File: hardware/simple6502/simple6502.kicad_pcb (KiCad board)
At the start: 2 copper layers, 100 x 100 mm, 37 parts, among them J1 ~{VP}, J2 CLK SEL, J3 RESET, J5 POWER 5V, J6 AUX 5VDC, SW1 RESET, SW2 POWER, T1 DS1813-10+, U1 W65C02SxP, U2 CY62256-70PC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

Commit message: First PCB Layout
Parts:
- moved U4 139.9 mm to (62.4, 115.5)
- moved U5 139.6 mm to (62.3, 102.6)
- moved C7 86.4 mm to (116.5, 54.0), turned to 180 degrees
- moved C6 86.1 mm to (124.0, 83.0), turned to -90 degrees
- moved TP3 74.5 mm to (114.0, 145.0)
- moved C3 64.5 mm to (82.5, 120.5), turned to -90 degrees
- moved C2 54.4 mm to (86.8, 94.0)
- moved C1 53.5 mm to (55.5, 74.0)
- moved TP1 49.0 mm to (134.0, 119.0)
- moved J2 47.7 mm to (141.0, 119.0), turned to 90 degrees
- moved TP2 47.6 mm to (137.0, 54.5)
- moved R3 45.0 mm to (117.0, 70.2), turned to -90 degrees
- moved R2 40.5 mm to (120.5, 70.2), turned to -90 degrees
- moved C5 31.5 mm to (55.8, 108.0)
- moved R5 30.3 mm to (147.5, 67.6), turned to 90 degrees
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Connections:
- net Net-(U1-BE) renamed /BE
- net Net-(U1-~{SO}) renamed /~{SO}
- R3 pad 1: VCC -> /RDY
- R3 pad 2: Net-(U1-RDY) -> VCC
- U1 pad 2: Net-(U1-RDY) -> /RDY

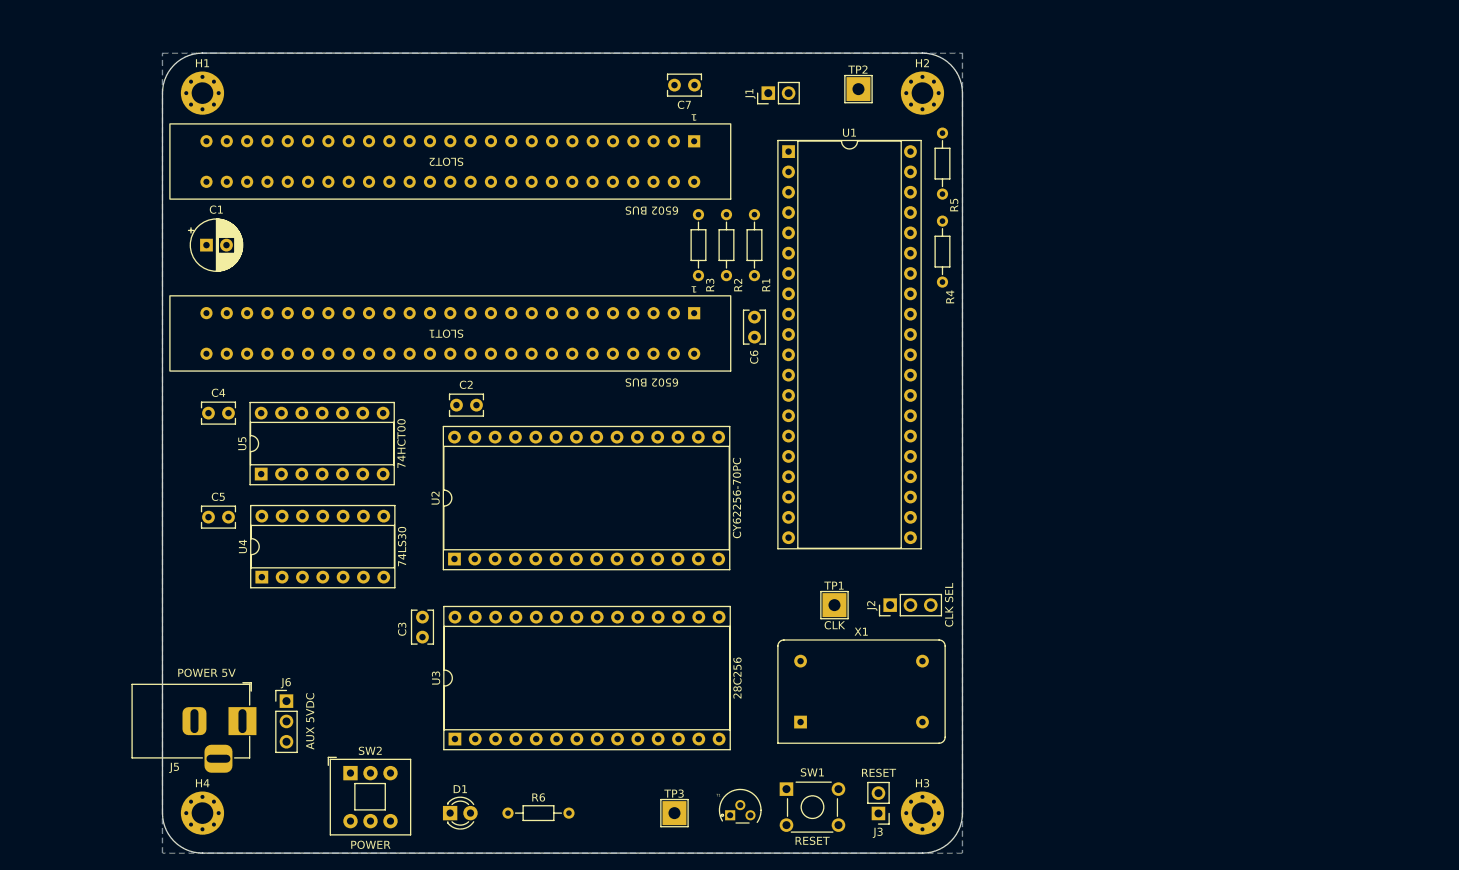
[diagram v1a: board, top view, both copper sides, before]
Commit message: Fixed Apple Connector 3D model, routing started
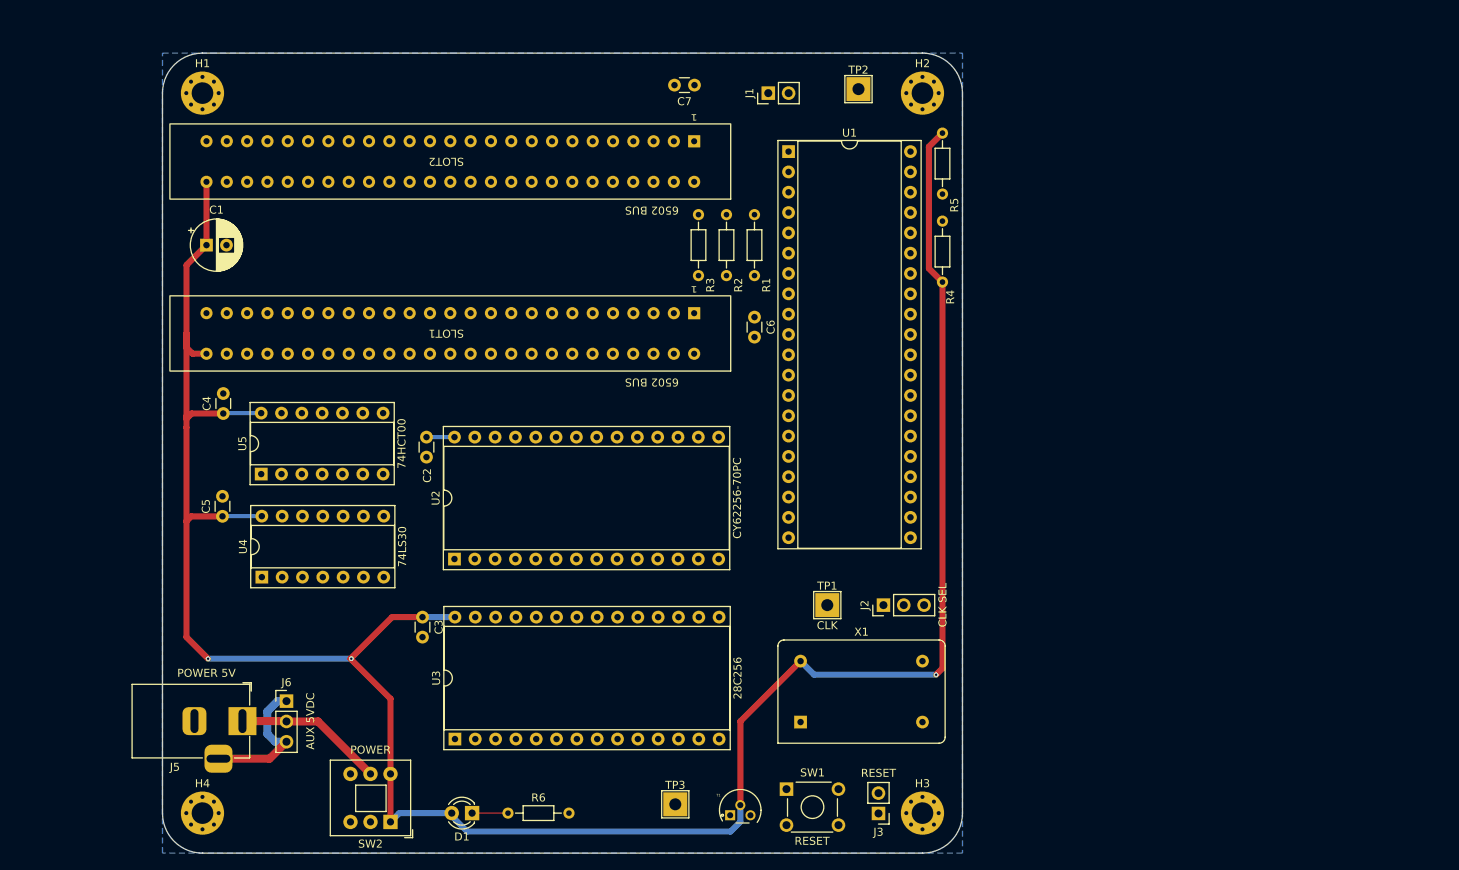
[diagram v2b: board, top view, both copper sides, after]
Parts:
- C2, C3, C4, C5, C6, C7: footprint Capacitor_THT:C_Rect_L4.0mm_W2.5mm_P2.50mm -> Capacitor_THT:C_Disc_D3.0mm_W1.6mm_P2.50mm
- moved SW2 7.89 mm to (78.5, 146.1), turned to 180 degrees
- moved C2 5.48 mm to (83.0, 98.0), turned to -90 degrees
- moved D1 2.74 mm to (88.7, 145.0), turned to 180 degrees
- moved C4 1.85 mm to (57.6, 95.0), turned to 90 degrees
- moved C5 1.75 mm to (57.5, 107.9), turned to 90 degrees
- moved TP3 1.10 mm to (114.1, 143.9)
- moved TP1 0.90 mm to (133.1, 119.0)
- moved J2 0.84 mm to (140.1, 119.0)
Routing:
- net VCC: track 0.00 -> 300.9 mm, vias 0 -> 3
- net /Power and support/5VDC IN: track 0.00 -> 18.7 mm
- net /Power and support/AUX GND: track 0.00 -> 17.9 mm
- net Net-(D1-K): track 0.00 -> 4.49 mm

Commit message: Routing PCB
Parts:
- moved C6 2.30 mm to (124.0, 80.7)
- moved R4 1.50 mm to (147.5, 72.5)
- moved R5 0.22 mm to (147.5, 67.4)
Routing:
- net A10: track 0.00 -> 80.1 mm, vias 0 -> 2
- net A11: track 0.00 -> 77.9 mm, vias 0 -> 2
- net A13: track 0.00 -> 75.2 mm, vias 0 -> 1
- net CLK: track 0.00 -> 73.0 mm
- net A8: track 0.00 -> 72.4 mm, vias 0 -> 2
- net A14: track 0.00 -> 70.7 mm
- net A9: track 0.00 -> 70.1 mm, vias 0 -> 2
- net A12: track 0.00 -> 66.8 mm, vias 0 -> 1
- net VCC: track 300.9 -> 347.4 mm
- net D7: track 0.00 -> 46.2 mm
- net A1: track 0.00 -> 45.8 mm
- net D5: track 0.00 -> 45.7 mm
- net D4: track 0.00 -> 45.7 mm
- net ~{RD}: track 0.00 -> 45.7 mm
- net D3: track 0.00 -> 45.7 mm
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
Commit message: More PCB Routing
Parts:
- moved J3 88.3 mm to (139.8, 56.7)
- moved R6 29.4 mm to (66.4, 132.8), turned to 90 degrees
- moved TP3 25.1 mm to (139.2, 142.7)
- moved D1 21.1 mm to (71.5, 132.8), turned to 0 degrees
- moved J6 10.2 mm to (62.0, 140.6)
- moved C3 9.16 mm to (83.0, 111.3)
- moved U3 9.14 mm to (86.6, 126.6)
- moved SW1 8.06 mm to (134.4, 146.9), turned to 180 degrees
- moved U4 7.97 mm to (55.8, 111.1)
- moved U5 7.25 mm to (55.8, 99.5)
- moved C5 6.40 mm to (52.9, 103.5), turned to -90 degrees
- moved C2 6.15 mm to (82.9, 91.8)
- moved U2 6.14 mm to (86.5, 107.1)
- moved C4 5.66 mm to (52.9, 91.9), turned to -90 degrees
- moved SW2 3.50 mm to (75.2, 145.1)
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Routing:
- net ~{RESET}: track 29.7 -> 130.1 mm
- net D6: track 22.3 -> 99.9 mm, vias 0 -> 2
- net A14: track 70.7 -> 122.3 mm, vias 0 -> 2
- net D2: track 45.6 -> 94.1 mm, vias 0 -> 2
- net D7: track 46.2 -> 94.6 mm, vias 0 -> 2
- net D5: track 45.7 -> 92.8 mm, vias 0 -> 2
- net D4: track 45.7 -> 92.7 mm, vias 0 -> 2
- net D1: track 45.6 -> 90.5 mm, vias 0 -> 2
- net D3: track 45.7 -> 90.4 mm, vias 0 -> 1
- net A7: track 45.7 -> 87.2 mm, vias 0 -> 1
- net D0: track 45.6 -> 86.0 mm, vias 0 -> 2
- net A6: track 45.7 -> 82.6 mm, vias 0 -> 1
- net A5: track 45.7 -> 78.3 mm, vias 0 -> 1
- net A11: track 77.9 -> 49.0 mm, vias 2 -> 0
- net A4: track 45.7 -> 73.8 mm, vias 0 -> 1
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
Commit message: Much More PCB Routing - Clean DRC
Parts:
- T1: value DS1813-10+ -> DS1813
- moved C1 0.96 mm to (55.4, 73.0), turned to -90 degrees
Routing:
- net GND: track 22.4 -> 0.00 mm
- net VCC: track 366.9 -> 368.3 mm
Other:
- board text added: "5V"
- board text added: "GND"
- board text added: "SW-G"
- board text added: "~{RESET}"

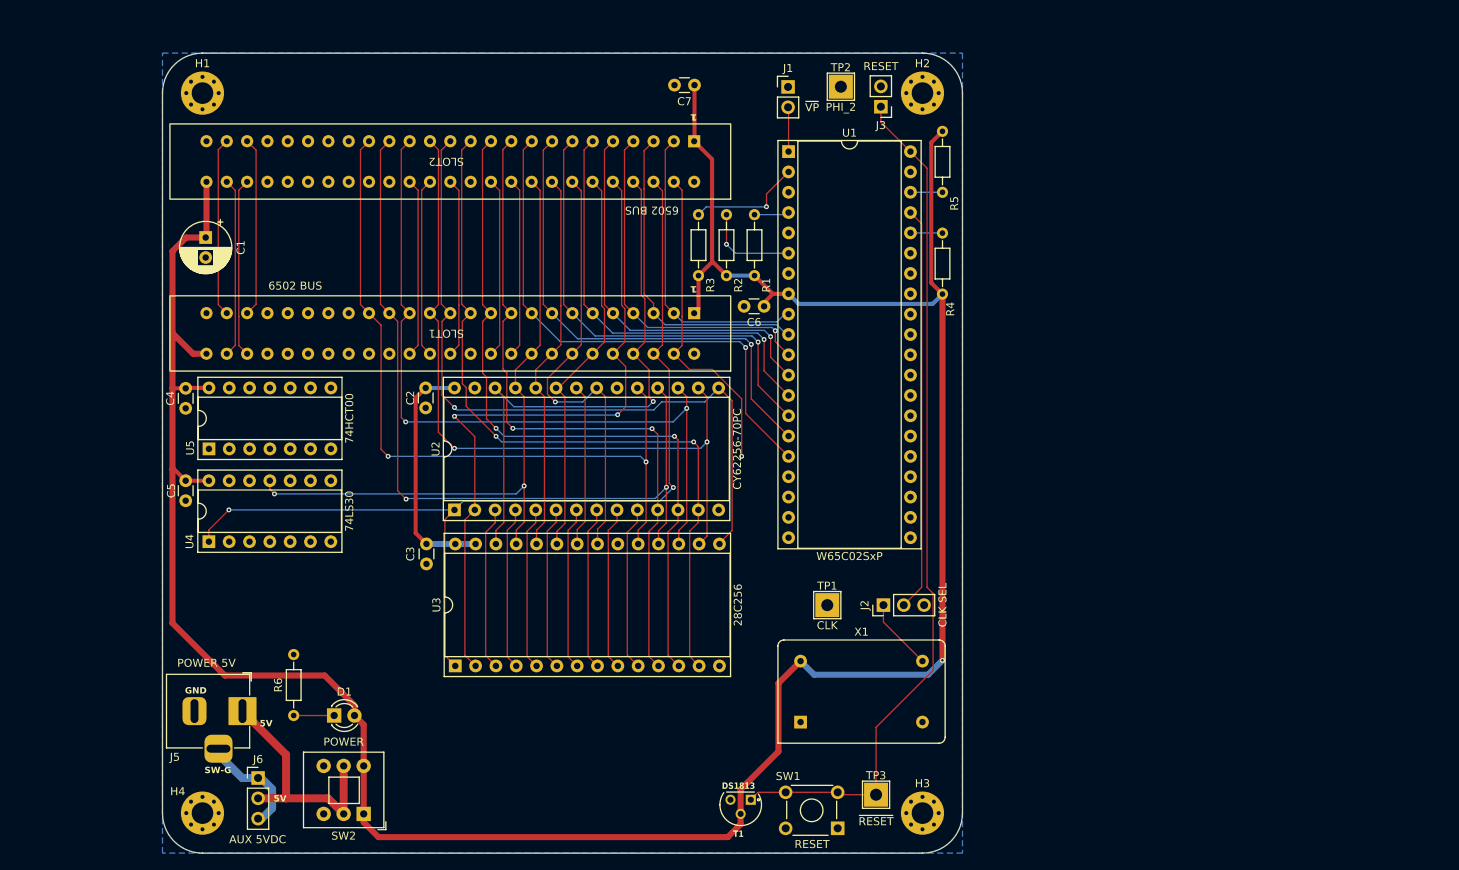
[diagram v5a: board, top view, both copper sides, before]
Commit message: Mostly done, Address and Data finished
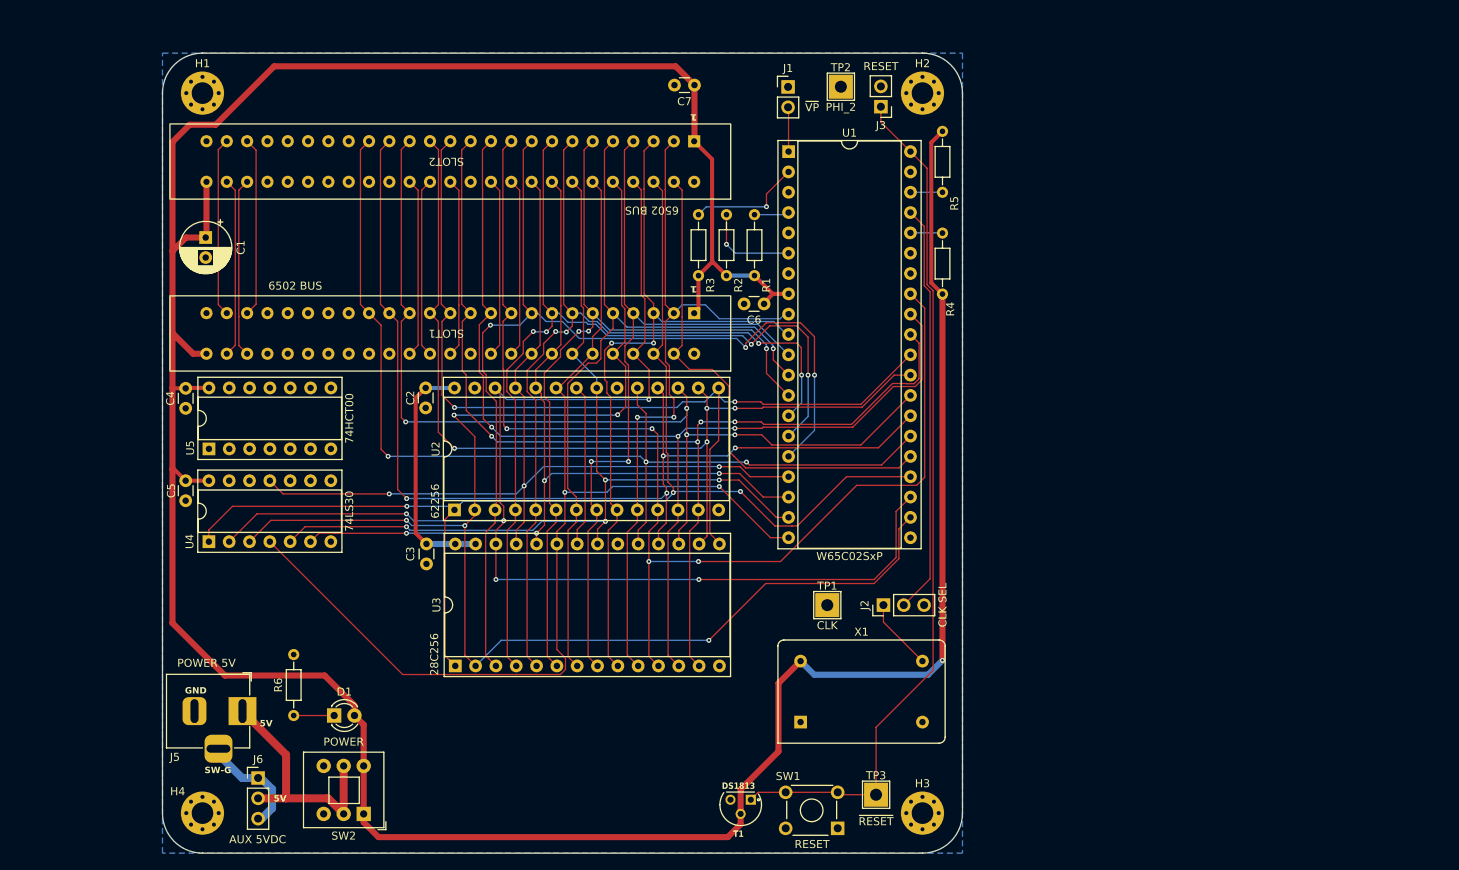
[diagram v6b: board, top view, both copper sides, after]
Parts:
- U2: value CY62256-70PC -> 62256
- moved C6 0.30 mm to (125.2, 81.3)
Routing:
- net A13: track 71.1 -> 169.4 mm, vias 1 -> 5
- net A12: track 85.2 -> 177.9 mm, vias 2 -> 5
- net A11: track 49.4 -> 140.2 mm, vias 0 -> 2
- net VCC: track 368.3 -> 431.5 mm
- net D0: track 86.0 -> 149.0 mm, vias 2 -> 4
- net A9: track 47.9 -> 108.7 mm, vias 0 -> 4
- net A10: track 56.4 -> 114.2 mm, vias 1 -> 4
- net D1: track 90.6 -> 133.6 mm, vias 2 -> 3
- net A7: track 87.2 -> 128.7 mm, vias 1 -> 3
- net D2: track 94.2 -> 133.2 mm, vias 2 -> 4
- net A6: track 82.7 -> 119.8 mm, vias 1 -> 4
- net A14: track 122.4 -> 157.2 mm, vias 2 -> 3
- net D7: track 94.2 -> 128.9 mm, vias 2 -> 3
- net A8: track 81.4 -> 115.3 mm, vias 2 -> 3
- net D6: track 100.0 -> 132.6 mm, vias 2 -> 4
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
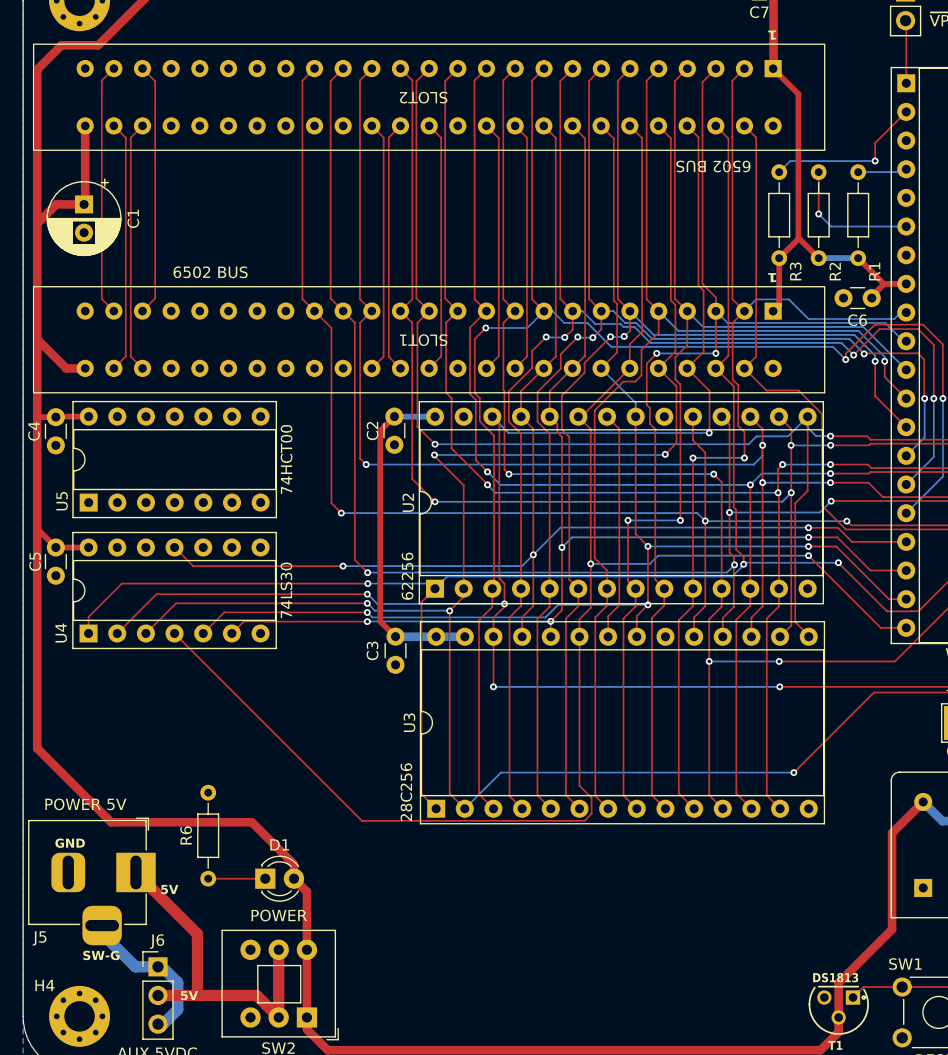
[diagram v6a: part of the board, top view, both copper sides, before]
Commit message: rearange the bus for better routing
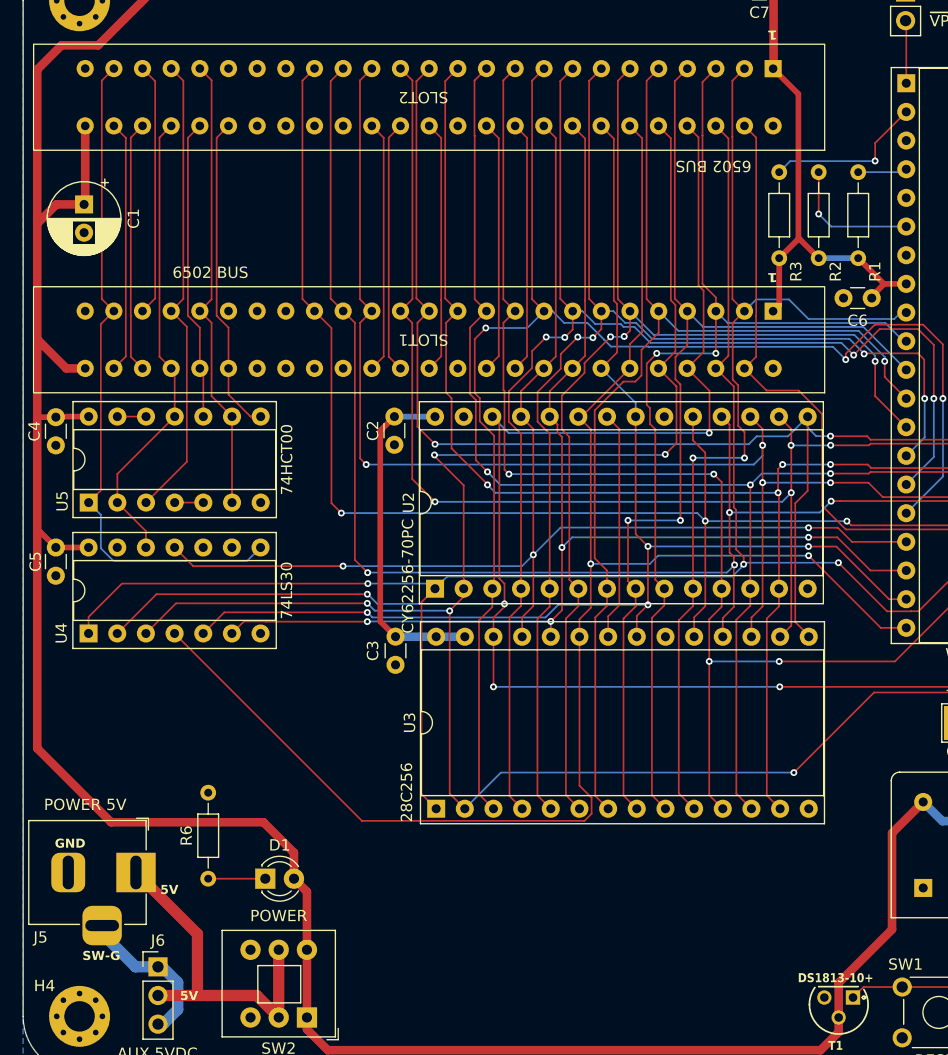
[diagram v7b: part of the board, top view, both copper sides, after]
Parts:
- T1: value DS1813 -> DS1813-10+
- U2: value 62256 -> CY62256-70PC
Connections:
- SLOT1 pad 21: unconnected-(SLOT1-Pin_21-Pad21) -> ~{RD}
- SLOT1 pad 22: unconnected-(SLOT1-Pin_22-Pad22) -> ~{RAM_CS}
- SLOT1 pad 24: CLK -> ~{IO_CS}
- SLOT1 pad 29: unconnected-(SLOT1-Pin_29-Pad29) -> ~{ROM_CS}
- SLOT1 pad 30: unconnected-(SLOT1-Pin_30-Pad30) -> CLK
- SLOT1 pad 31: unconnected-(SLOT1-Pin_31-Pad31) -> ~{WR}
- SLOT1 pad 36: ~{IO_CS} -> unconnected-(SLOT1-Pin_36-Pad36)
- SLOT1 pad 37: ~{ROM_CS} -> unconnected-(SLOT1-Pin_37-Pad37)
- SLOT1 pad 38: ~{RAM_CS} -> unconnected-(SLOT1-Pin_38-Pad38)
- SLOT1 pad 40: ~{WR} -> unconnected-(SLOT1-Pin_40-Pad40)
- SLOT1 pad 41: ~{RD} -> unconnected-(SLOT1-Pin_41-Pad41)
- SLOT2 pad 21: unconnected-(SLOT2-Pin_21-Pad21) -> ~{RD}
- SLOT2 pad 22: unconnected-(SLOT2-Pin_22-Pad22) -> ~{RAM_CS}
- SLOT2 pad 24: CLK -> ~{IO_CS}
- SLOT2 pad 29: unconnected-(SLOT2-Pin_29-Pad29) -> ~{ROM_CS}
- SLOT2 pad 30: unconnected-(SLOT2-Pin_30-Pad30) -> CLK
- SLOT2 pad 31: unconnected-(SLOT2-Pin_31-Pad31) -> ~{WR}
- SLOT2 pad 36: ~{IO_CS} -> unconnected-(SLOT2-Pin_36-Pad36)
- SLOT2 pad 37: ~{ROM_CS} -> unconnected-(SLOT2-Pin_37-Pad37)
- SLOT2 pad 38: ~{RAM_CS} -> unconnected-(SLOT2-Pin_38-Pad38)
- SLOT2 pad 40: ~{WR} -> unconnected-(SLOT2-Pin_40-Pad40)
- SLOT2 pad 41: ~{RD} -> unconnected-(SLOT2-Pin_41-Pad41)
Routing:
- net ~{IO_CS}: track 22.4 -> 82.2 mm
- net ~{ROM_CS}: track 22.4 -> 63.9 mm
- net ~{RAM_CS}: track 22.4 -> 63.8 mm
- net ~{RD}: track 42.7 -> 83.2 mm
- net ~{WR}: track 22.4 -> 50.7 mm
- net CLK: track 73.8 -> 78.2 mm
- net R~{W}: track 0.00 -> 2.54 mm
- net A15: track 63.2 -> 65.7 mm
- net VCC: track 431.5 -> 432.1 mm
